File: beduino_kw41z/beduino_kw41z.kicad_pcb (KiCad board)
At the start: 2 copper layers, 65 x 19 mm, 57 parts, among them J1 USB_OTG, J2 Conn_01x07, J3 Conn_01x07, Q1 Q_PMOS_SGD, SW1 SW_Push, SW2 Reset, U1 TC1017, U2 LPC11U35FHI33-501, U3 TC1017, U4 Module_CONN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

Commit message: Small improvements to the PCB design.
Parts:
- moved C11 0.70 mm to (111.0, 52.0)
- moved ANT1 0.67 mm to (118.1, 53.4)
- moved C17 0.65 mm to (101.3, 54.6), turned to 270 degrees
- moved Y2 0.60 mm to (109.6, 55.2), turned to 0 degrees
- moved L1 0.31 mm to (111.8, 53.5)
- moved C10 0.15 mm to (113.2, 54.8)
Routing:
- net GND: track 92.5 -> 75.3 mm, vias 39 -> 34
- net +3V3: track 139.7 -> 126.0 mm, vias 8 -> 5
- net Net-(U5-Pad30): track 6.90 -> 4.61 mm
- net /DIPDAP/TGT_TX: track 47.4 -> 45.7 mm
- net /DIPDAP/TGT_RX: track 53.3 -> 51.6 mm
- net Net-(ANT1-Pad1): track 2.08 -> 3.04 mm
- net Net-(U5-Pad31): track 2.35 -> 2.88 mm

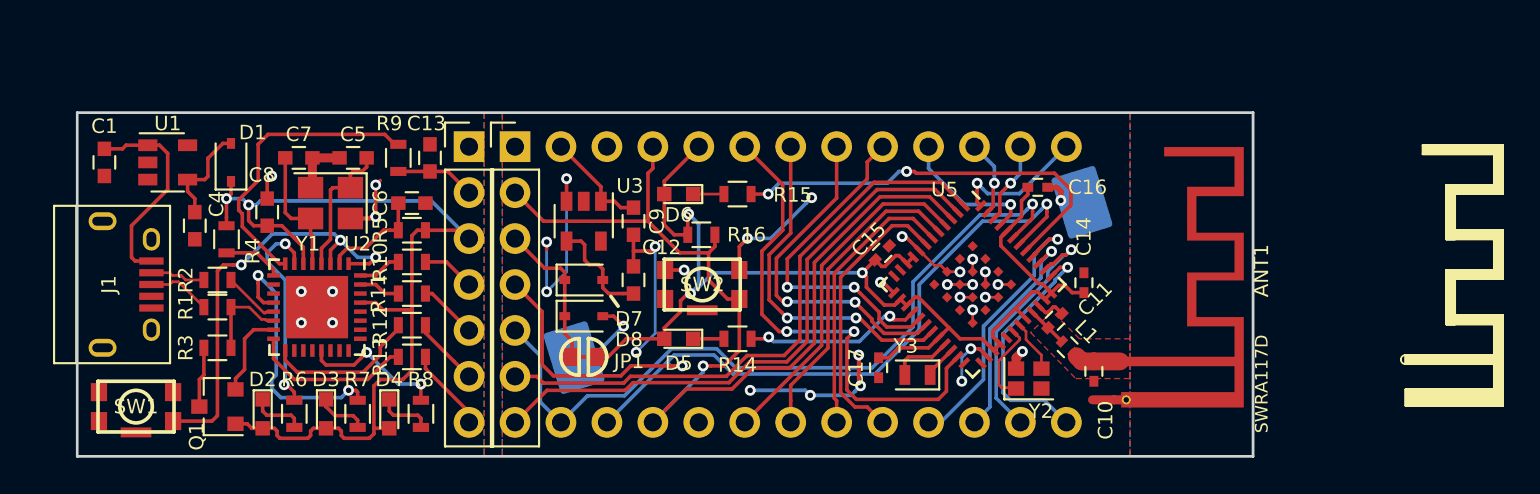
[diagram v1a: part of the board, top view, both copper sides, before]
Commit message: Add panelized pcb
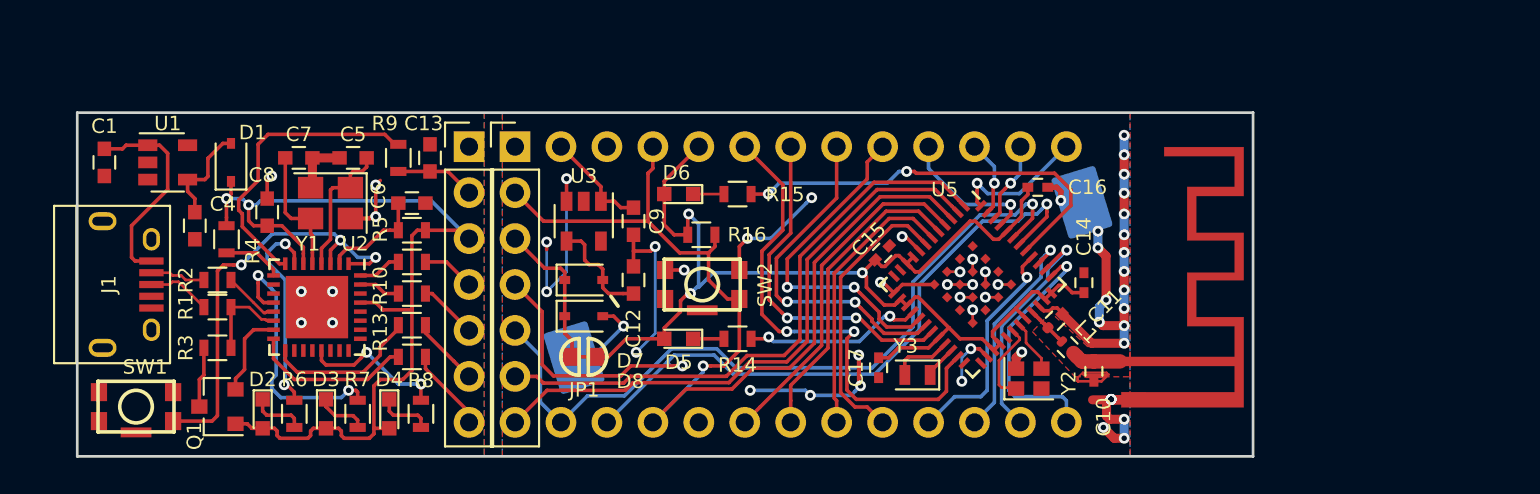
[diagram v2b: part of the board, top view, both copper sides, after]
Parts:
- added REF***: OSHW-Symbol_6.7x6mm_SilkScreen, Symbols:OSHW-Symbol_6.7x6mm_SilkScreen, B.Cu at (86.7, 50.0)
- renumbered R12 to R13-R10
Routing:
- net GND: track 75.3 -> 109.9 mm, vias 34 -> 57
- net /KW41Z/D6: track 15.6 -> 12.6 mm
- net +3V3: track 126.0 -> 128.6 mm
- net /KW41Z/ANT: track 2.32 -> 3.56 mm
- net /KW41Z/SCL: track 13.8 -> 13.1 mm
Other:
- board text added: "10/ PTC19"
- board text added: "2/ PTA16"
- board text added: "3/ PTA17"
- board text added: "4/ PTA18"
- board text added: "5/ PTA19"
- board text added: "6/ PTC4"
- board text added: "9/ PTC1"
- board text added: "A0/ PTB1"
- board text added: "A1/ PTB2"
- board text added: "A2/ PTB3"
- board text added: "A3/ PTB18"
- board text added: "GND"
- board text added: "MISO/ PTC18"
- board text added: "MOSI/ PTC17"
- board text added: "RST"
- board text added: "RX"
- board text added: "SCK/ PTC16"
- board text added: "SCL/ PTC2"
- board text added: "SDA/ PTC3"
- board text added: "TX"
- board text added: "VCC"
- board text added: "VIN"

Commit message: Update board design to be kicad v4 compatible again.
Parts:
- Q1: value Q_PMOS_SGD -> BSS84

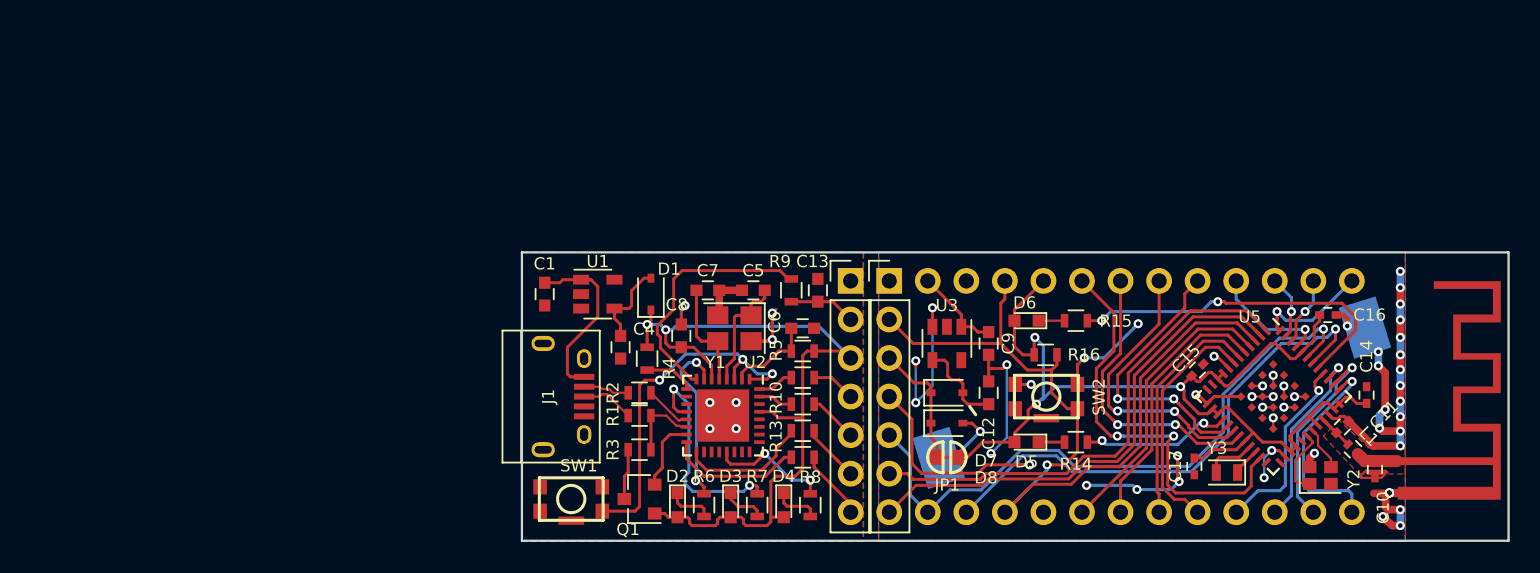
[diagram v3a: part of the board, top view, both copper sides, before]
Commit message: Update PCB layout.
The connection between the dipdap and the kw41z-mini is now closed with
a small trace. If the trace is cut, added smd pads simplify the creation
of solder jumpers.
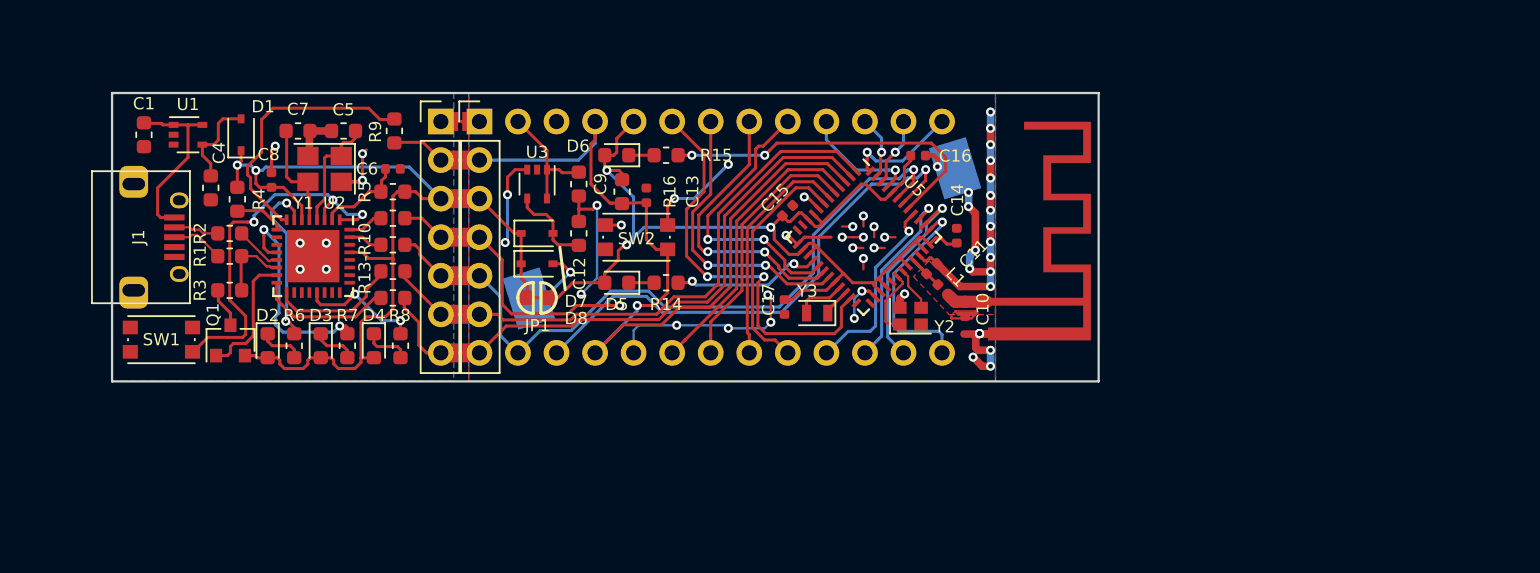
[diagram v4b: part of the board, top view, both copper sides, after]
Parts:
- removed REF***: OSHW-Symbol_6.7x6mm_SilkScreen, Symbols:OSHW-Symbol_6.7x6mm_SilkScreen
- C1, C12, C4, C5, C7, C9: footprint Capacitors_SMD:C_0603 -> Capacitor_SMD:C_0603_1608Metric
- C10, C11, C14, C15, C16, C17: footprint Capacitors_SMD:C_0402 -> Capacitor_SMD:C_0402_1005Metric
- C13, C6, C8: footprint Capacitors_SMD:C_0603 -> Capacitor_SMD:C_0402_1005Metric
- D1, D7, D8: footprint Diodes_SMD:D_SOD-323 -> Diode_SMD:D_SOD-323
- D2, D3, D4, D5, D6: footprint LEDs:LED_0603 -> LED_SMD:LED_0603_1608Metric
- L1: footprint Inductors_SMD:L_0402 -> Inductor_SMD:L_0402_1005Metric
- Q1: value BSS84 -> Q_PMOS_GSD; footprint TO_SOT_Packages_SMD:SOT-23 -> Package_TO_SOT_SMD:SOT-23
- R1, R10, R11, R13, R13-R10, R14, R15, R16, R2, R3, R4, R5, R6, R7, R8, R9: footprint Resistors_SMD:R_0603 -> Resistor_SMD:R_0603_1608Metric
- SW1, SW2: footprint button:SW_SPST_KMR6 -> Button_Switch_SMD:SW_SPST_KMR2
- U1, U3: footprint TO_SOT_Packages_SMD:SOT-23-5 -> Package_TO_SOT_SMD:SOT-353_SC-70-5
- U2: footprint Housings_DFN_QFN:QFN-32-1EP_5x5mm_Pitch0.5mm -> Package_DFN_QFN:QFN-32-1EP_5x5mm_P0.5mm_EP3.45x3.45mm
- U5: footprint Housings_DFN_QFN:QFN-48-1EP_7x7mm_Pitch0.5mm -> Package_DFN_QFN:QFN-48-1EP_7x7mm_P0.5mm_EP5.15x5.15mm
- Y1: footprint Crystals:Crystal_SMD_3225-4pin_3.2x2.5mm -> Crystal:Crystal_SMD_3225-4Pin_3.2x2.5mm
- Y2: footprint Crystals:Crystal_SMD_2016-4pin_2.0x1.6mm -> Crystal:Crystal_SMD_2016-4Pin_2.0x1.6mm
- Y3: footprint Crystals:Crystal_SMD_2012-2pin_2.0x1.2mm -> Crystal:Crystal_SMD_2012-2Pin_2.0x1.2mm
- moved R16 29.9 mm to (63.6, 36.5), turned to 270 degrees
- moved D6 29.1 mm to (63.2, 34.1)
- moved R15 29.1 mm to (66.5, 34.1)
- moved C11 29.0 mm to (84.0, 41.6)
- moved C10 29.0 mm to (86.2, 44.2)
- moved ANT1 29.0 mm to (91.1, 42.9)
- moved BT1 29.0 mm to (71.5, 39.2)
- moved C12 29.0 mm to (60.8, 39.2)
- moved C14 29.0 mm to (85.7, 39.4)
- moved C15 29.0 mm to (74.5, 37.8)
- moved C16 29.0 mm to (83.1, 34.1)
- moved C17 29.0 mm to (74.3, 44.1)
- moved C4 29.0 mm to (36.5, 36.2)
- moved C5 29.0 mm to (45.2, 32.5)
- moved C6 29.0 mm to (48.5, 35.0)
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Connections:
- net /DIPDAP/USB_N renamed Net-(J1-Pad2)
- net /DIPDAP/USB_P renamed Net-(J1-Pad3)
- net /DIPDAP/USB_R_N renamed Net-(C2-Pad1)
- net /DIPDAP/USB_R_P renamed Net-(C3-Pad1)
- Q1 pad 1: +3V3 -> Net-(Q1-Pad1)
- Q1 pad 2: Net-(Q1-Pad2) -> +3V3
- U1 pad 5: (no net) -> VBUS
- U2 pad 15: Net-(Q1-Pad2) -> Net-(Q1-Pad1)
- U3 pad 5: (no net) -> VCC
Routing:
- net Net-(Q1-Pad1): track 0.00 -> 8.54 mm
- net Net-(Q1-Pad2): track 4.81 -> 0.00 mm
- net /DIPDAP/TGT_SWCLK: track 37.6 -> 40.7 mm
- net /DIPDAP/TGT_TX: track 45.7 -> 48.8 mm
- net +3V3: track 128.6 -> 131.7 mm
- net /DIPDAP/TGT_NRESET: track 59.8 -> 62.3 mm
- net /DIPDAP/TGT_SWDIO: track 36.7 -> 39.2 mm
- net /DIPDAP/TGT_RX: track 51.6 -> 54.2 mm
- net VCC: track 6.13 -> 8.15 mm
- net Net-(SW1-Pad2): track 23.9 -> 25.2 mm
- net GND: track 109.9 -> 111.0 mm, vias 57 -> 56
- net Net-(R9-Pad2): track 16.5 -> 17.6 mm
- net Net-(Q1-Pad3): track 3.35 -> 2.63 mm
- net Net-(C4-Pad1): track 5.53 -> 6.23 mm
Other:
- board text added: "*=ADC"
- board text added: "*PTB1"
- board text added: "*PTB18"
- board text added: "*PTB2"
- board text added: "*PTB3"
- board text added: "+=SPI"
- board text added: "+PTC16"
- board text added: "+PTC17"
- board text added: "+PTC18"
- board text added: "-=I2C"
- board text added: "-PTC19"
- board text added: "Beduino-Pro-Mini"
- board text added: "PTA16+"
- board text added: "PTA17+"
- board text added: "PTA18+"
- board text added: "PTA19"
- board text added: "PTC1-"
- board text added: "PTC2-"
- board text added: "PTC3-"
- board text added: "PTC4"
- board text added: "SWCLK"
- board text added: "SWDIO"
- board text added: "v1.1"
- board text removed: "10/ PTC19"
- board text removed: "2/ PTA16"
- board text removed: "3/ PTA17"
- board text removed: "4/ PTA18"
- board text removed: "5/ PTA19"
- board text removed: "6/ PTC4"
- board text removed: "9/ PTC1"
- board text removed: "A0/ PTB1"
- board text removed: "A1/ PTB2"
- board text removed: "A2/ PTB3"
- board text removed: "A3/ PTB18"
- board text removed: "MISO/ PTC18"
- board text removed: "MOSI/ PTC17"
- board text removed: "SCK/ PTC16"
- board text removed: "SCL/ PTC2"
- board text removed: "SDA/ PTC3"
